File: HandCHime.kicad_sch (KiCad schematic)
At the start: 18 parts, among them J1 USB_C_Receptacle_USB2.0, J2 Pins, SW0 BOOT, SW1 Row 0, Col 0, SW2 Row 0, Col 1, U1 CH552T, U2 USBLC6-2P6

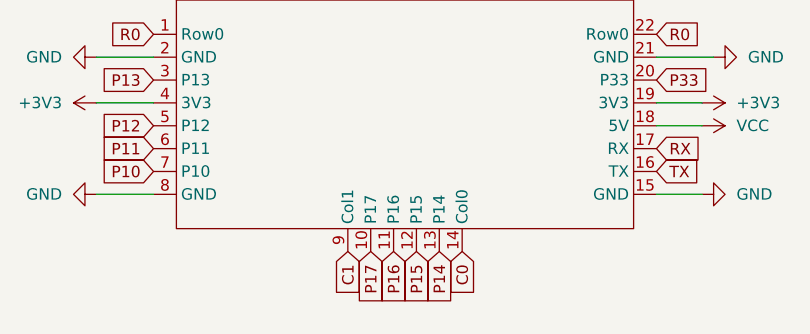
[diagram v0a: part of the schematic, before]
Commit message: Try moving MCU to central part of board
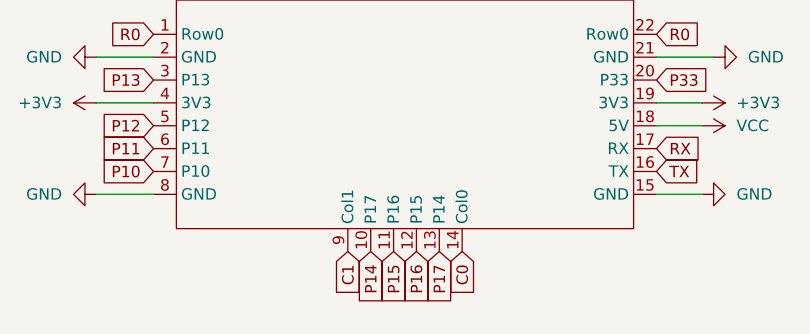
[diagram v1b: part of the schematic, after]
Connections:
- net P14: now also J2.10 (P17); no longer J2.13 (P14)
- net P15: now also J2.11 (P16); no longer J2.12 (P15)
- net P16: now also J2.12 (P15); no longer J2.11 (P16)
- net P17: now also J2.13 (P14); no longer J2.10 (P17)

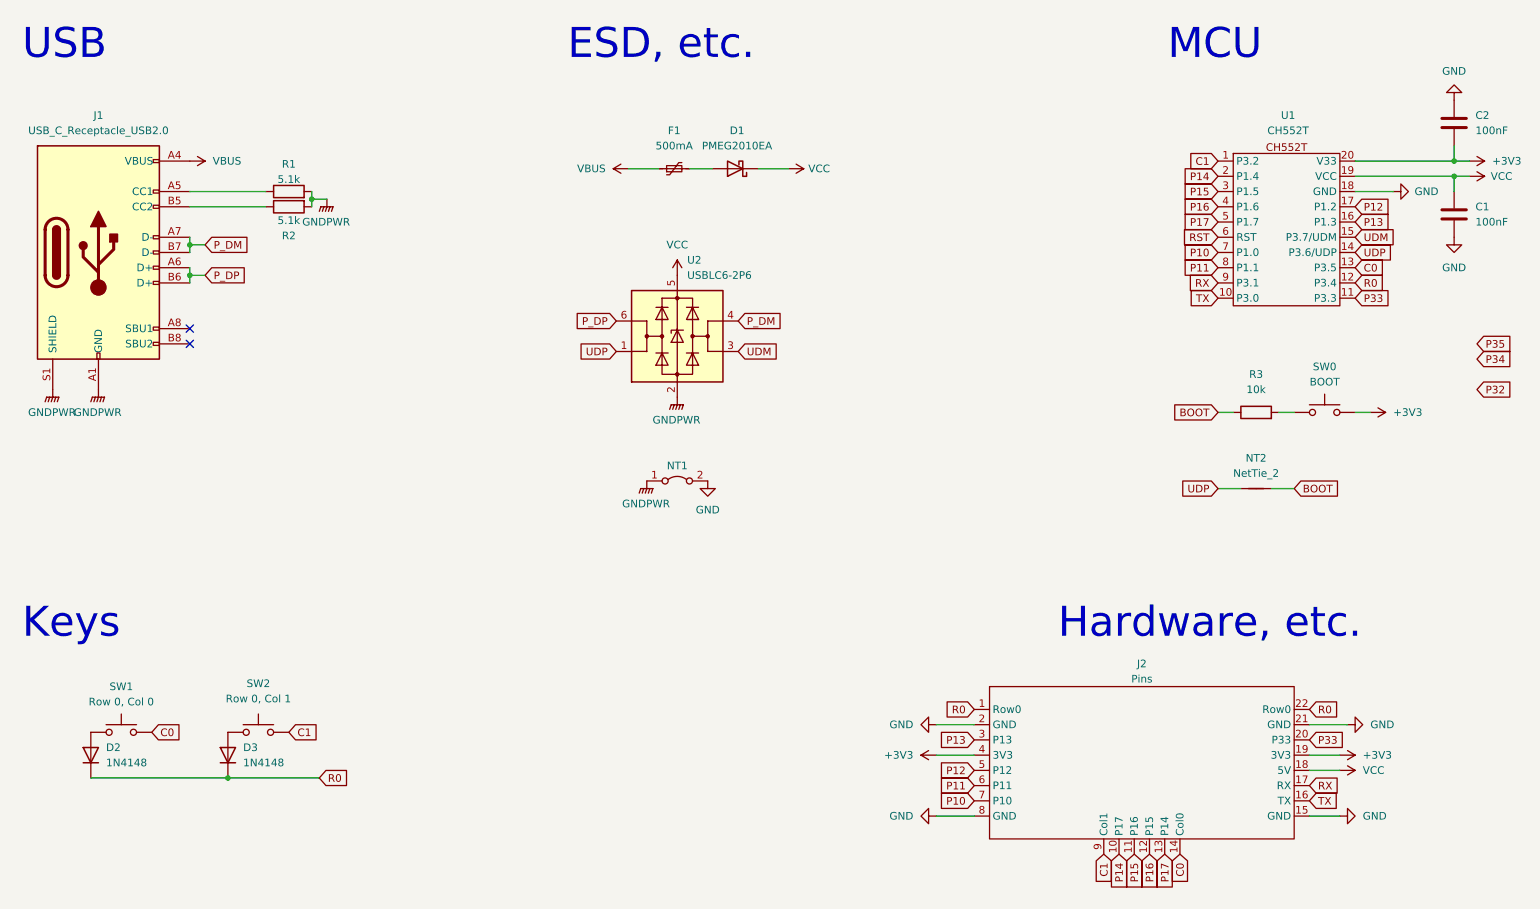
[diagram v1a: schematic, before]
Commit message: Move MCU to centre of board and reroute
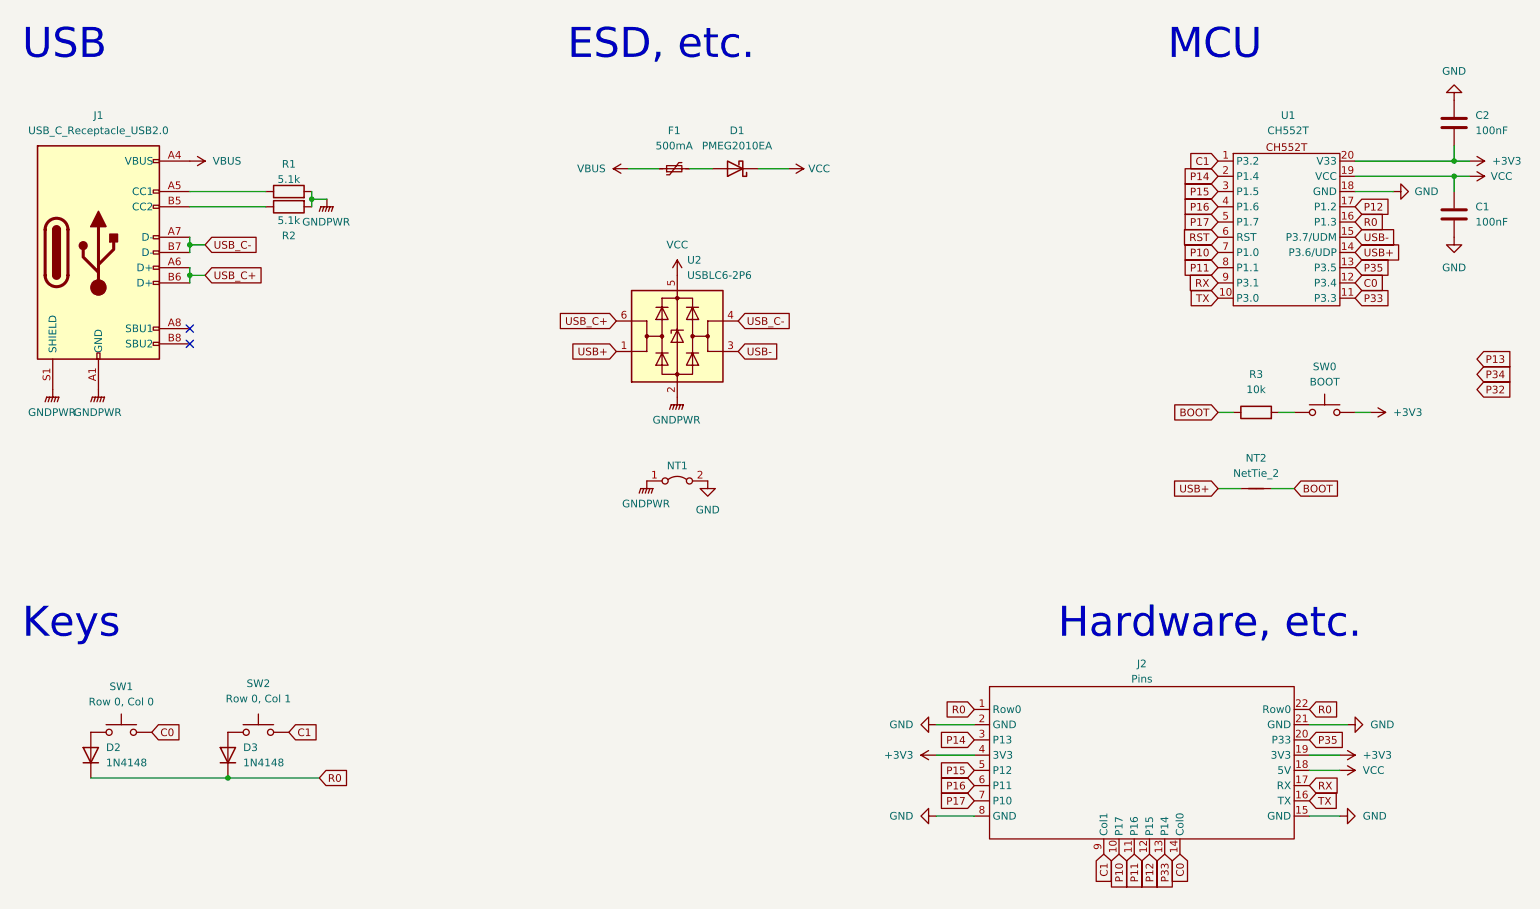
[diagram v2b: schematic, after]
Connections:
- net C0: now also U1.12 (P3.4); no longer U1.13 (P3.5)
- net P10: now also J2.10 (P17); no longer J2.7 (P10)
- net P11: now also J2.11 (P16); no longer J2.6 (P11)
- net P12: now also J2.12 (P15); no longer J2.5 (P12)
- net P13: no longer J2.3 (P13), U1.16 (P1.3)
- net P14: now also J2.3 (P13); no longer J2.10 (P17)
- net P15: now also J2.5 (P12); no longer J2.11 (P16)
- net P16: now also J2.6 (P11); no longer J2.12 (P15)
- net P17: now also J2.7 (P10); no longer J2.13 (P14)
- net P33: now also J2.13 (P14); no longer J2.20 (P33)
- net P35: now also J2.20 (P33), U1.13 (P3.5)
- net R0: now also U1.16 (P1.3); no longer U1.12 (P3.4)
- net P_DM renamed USB_C-
- net P_DP renamed USB_C+
- net UDM renamed USB-
- net UDP renamed USB+

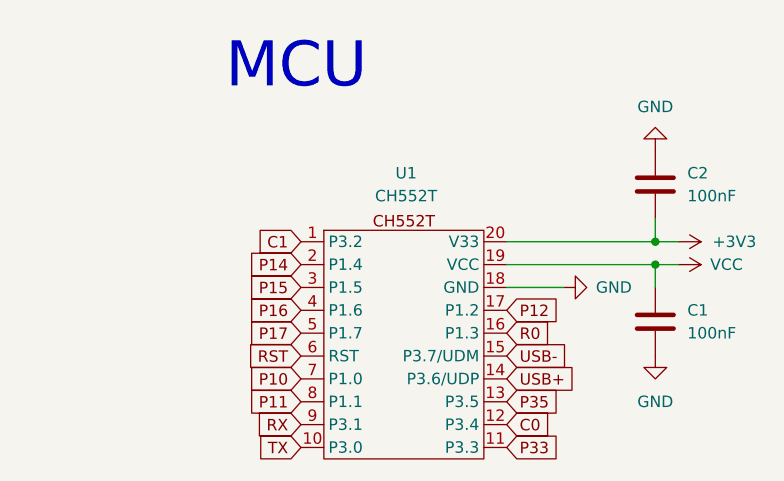
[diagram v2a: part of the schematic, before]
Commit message: Correct CH552 schematic symbols
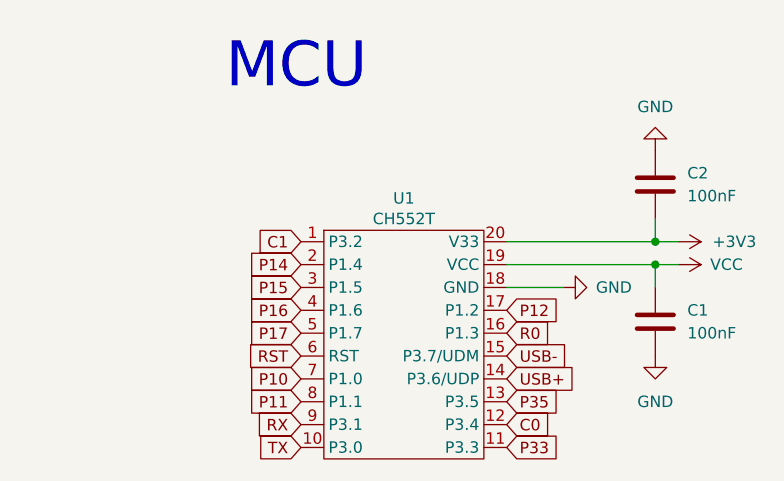
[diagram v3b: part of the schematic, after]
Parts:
- U1: symbol Project Library:MCU_CM552E_MSOP-10 -> Project Library:MCU_CH552T_TSSOP-20
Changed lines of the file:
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@@
 	)
 	(symbol
-		(lib_id "Project Library:MCU_CM552E_MSOP-10")
+		(lib_id "Project Library:MCU_CH552T_TSSOP-20")
 		(at 228.6 48.26 0)
 		(unit 1)
@@
 		(on_board yes)
 		(dnp no)
-		(fields_autoplaced yes)
 		(property "Reference" "U1"
-			(at 228.854 31.75 0)
+			(at 228.6 34.544 0)
 			(effects
 				(font
@@
 		)
 		(property "Value" "CH552T"
-			(at 228.854 34.29 0)
+			(at 228.6 36.83 0)
 			(effects
 				(font
@@
 			)
 		)
-		(property "Datasheet" ""
-			(at 228.6 60.96 0)
+		(property "Datasheet" "https://www.wch-ic.com/downloads/file/309.html"
+			(at 228.6 69.85 0)
 			(effects
 				(font
@@
 		)
 		(property "LCSC" "C111367"
-			(at 228.6 67.056 0)
+			(at 228.6 67.31 0)
 			(effects
 				(font

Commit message: Update net tie in schematic
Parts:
- NT2: footprint NetTie:NetTie-2_SMD_Pad0.5mm -> Project Library:NetTie-2_SMD_Pad0.254mm
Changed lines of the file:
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@@
 			)
 		)
-		(property "Footprint" "NetTie:NetTie-2_SMD_Pad0.5mm"
+		(property "Footprint" "Project Library:NetTie-2_SMD_Pad0.254mm"
 			(at 223.52 93.98 0)
 			(effects

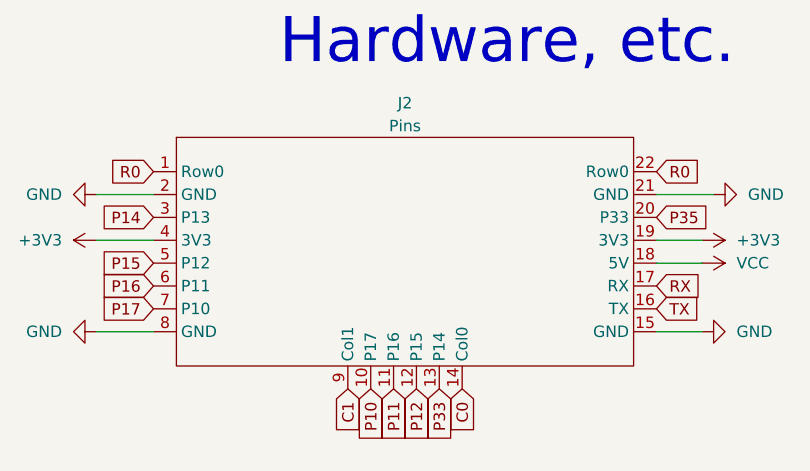
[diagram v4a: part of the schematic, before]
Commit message: Add labels to pins
Labels are currently on the back silkscreen, which is not the best. However, trying to squeeze them on the front seems optimistic.
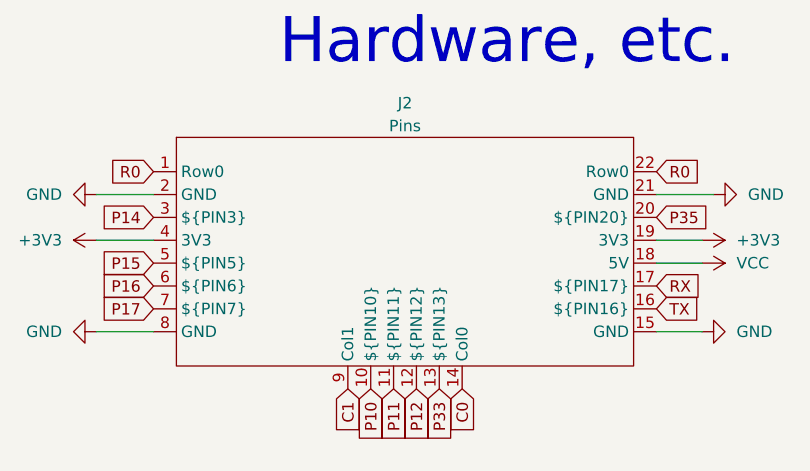
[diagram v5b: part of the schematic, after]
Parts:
- J2: PIN10 (none) -> 10; PIN11 (none) -> 11; PIN12 (none) -> 12; PIN13 (none) -> 33; PIN16 (none) -> 30(TX); PIN17 (none) -> 31(RX); PIN20 (none) -> 35; PIN3 (none) -> 14; PIN5 (none) -> 15; PIN6 (none) -> 16; PIN7 (none) -> 17
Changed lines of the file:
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@@
+			)
+		)
+		(property "PIN3" "14"
+			(at 204.47 139.7 0)
+			(effects
+				(font
+					(size 1.27 1.27)
+				)
+				(hide yes)
+			)
+		)
+		(property "PIN5" "15"
+			(at 204.47 139.7 0)
+			(effects
+				(font
+					(size 1.27 1.27)
+				)
+				(hide yes)
+			)
+		)
+		(property "PIN6" "16"
+			(at 204.47 139.7 0)
+			(effects
+				(font
+					(size 1.27 1.27)
+				)
+				(hide yes)
+			)
+		)
+		(property "PIN7" "17"
+			(at 204.47 139.7 0)
+			(effects
+				(font
+					(size 1.27 1.27)
+				)
+				(hide yes)
+			)
+		)
+		(property "PIN10" "10"
+			(at 204.47 139.7 0)
+			(effects
+				(font
+					(size 1.27 1.27)
+				)
+				(hide yes)
+			)
+		)
+		(property "PIN11" "11"
+			(at 204.47 139.7 0)
+			(effects
+				(font
+					(size 1.27 1.27)
+				)
+				(hide yes)
+			)
+		)
+		(property "PIN12" "12"
+			(at 204.47 139.7 0)
+			(effects
+				(font
+					(size 1.27 1.27)
+				)
+				(hide yes)
+			)
+		)
+		(property "PIN13" "33"
+			(at 204.47 139.7 0)
+			(effects
+				(font
+					(size 1.27 1.27)
+				)
+				(hide yes)
+			)
+		)
+		(property "PIN16" "30(TX)"
+			(at 204.47 139.7 0)
+			(effects
+				(font
+					(size 1.27 1.27)
+				)
+				(hide yes)
+			)
+		)
+		(property "PIN17" "31(RX)"
+			(at 204.47 139.7 0)
+			(effects
+				(font
+					(size 1.27 1.27)
+				)
+				(hide yes)
+			)
+		)
+		(property "PIN20" "35"
+			(at 204.47 139.7 0)
+			(effects
+				(font
+					(size 1.27 1.27)
+				)
+				(hide yes)
 			)
 		)

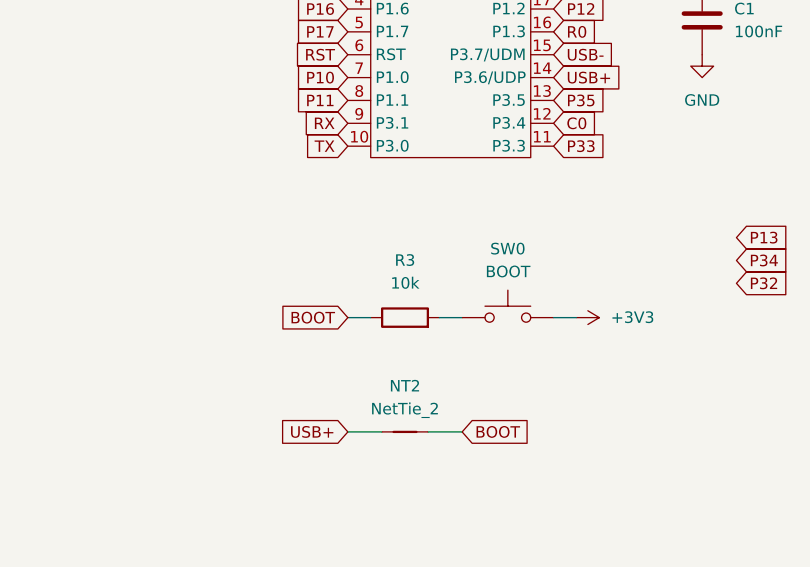
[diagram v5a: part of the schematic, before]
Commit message: Update boot switch
 * Now uses the smaller B3U-1000P switch
 * Alternate pads provided on the keyswitch side so that Boot can be accessed by removing a keycap and poking through LED slot (on compatible switches)
 * Can now reroute C0 to avoid snaking around too much
 * Took advantage of now smaller vias on other traces
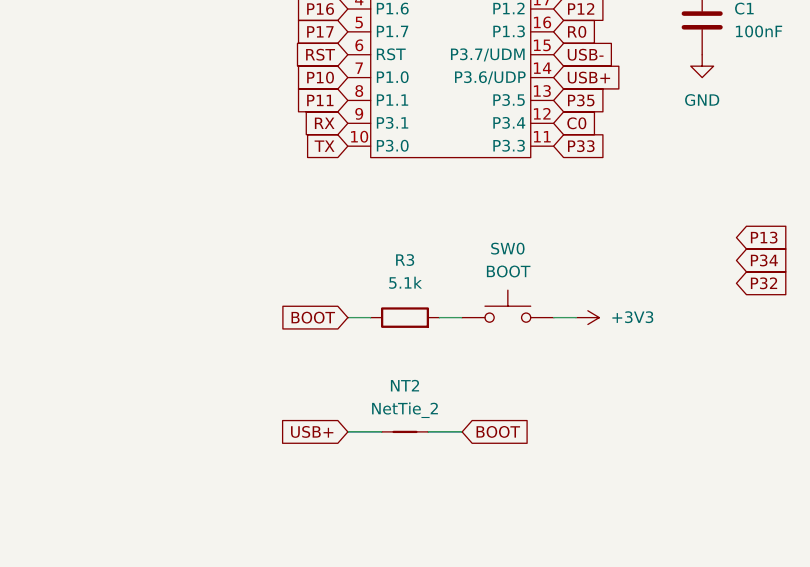
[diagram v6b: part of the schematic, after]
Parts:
- R3: value 10k -> 5.1k
- SW0: footprint PCM_marbastlib-various:SW_SPST_SKQG_WithStem -> Project Library:SW_SPST_B3U-1000P
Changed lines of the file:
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@@
 			)
 		)
-		(property "Value" "10k"
+		(property "Value" "5.1k"
 			(at 223.52 77.47 90)
 			(effects
@@
 			)
 		)
-		(property "Footprint" "PCM_marbastlib-various:SW_SPST_SKQG_WithStem"
+		(property "Footprint" "Project Library:SW_SPST_B3U-1000P"
 			(at 234.95 76.2 0)
 			(effects

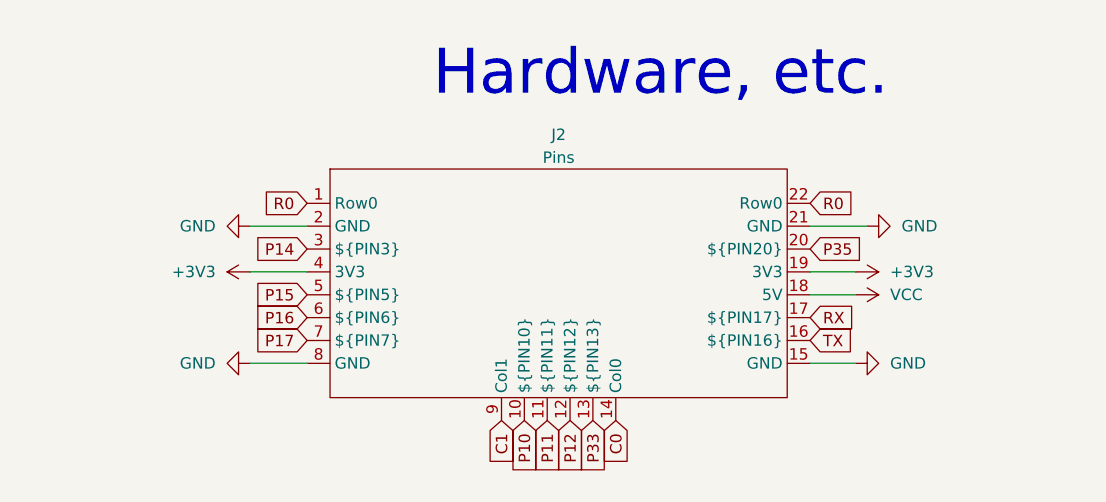
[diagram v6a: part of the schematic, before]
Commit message: Swap +5 and 3.3V outputs
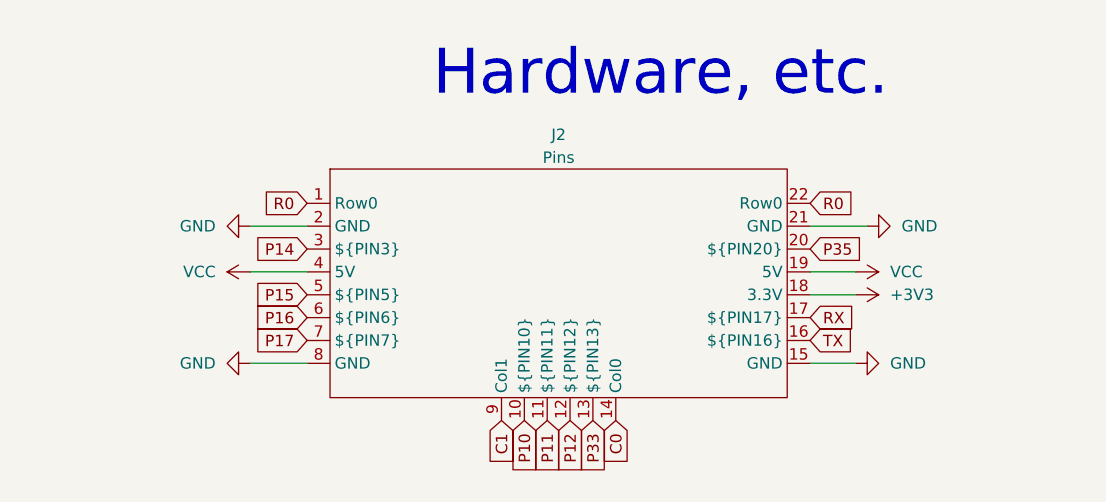
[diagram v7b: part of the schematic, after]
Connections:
- net +3V3: now also J2.18 (3.3V); no longer J2.19 (3V3), J2.4 (3V3)
- net VCC: now also J2.19 (5V), J2.4 (5V); no longer J2.18 (5V)
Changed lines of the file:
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@@
 	(symbol
 		(lib_id "power:+3V3")
-		(at 237.49 138.43 270)
-		(mirror x)
+		(at 237.49 140.97 270)
 		(unit 1)
 		(exclude_from_sim no)
@@
 		(dnp no)
 		(property "Reference" "#PWR011"
-			(at 233.68 138.43 0)
+			(at 233.68 140.97 0)
 			(effects
 				(font
@@
 		)
 		(property "Value" "+3V3"
-			(at 241.3 138.4299 90)
+			(at 241.3 140.9701 90)
 			(effects
 				(font
@@
 		)
 		(property "Footprint" ""
-			(at 237.49 138.43 0)
+			(at 237.49 140.97 0)
 			(effects
 				(font
@@
 		)
 		(property "Datasheet" ""
-			(at 237.49 138.43 0)
+			(at 237.49 140.97 0)
 			(effects
 				(font
@@
 		)
 		(property "Description" ""
-			(at 237.49 138.43 0)
+			(at 237.49 140.97 0)
 			(effects
 				(font
@@
 	)
 	(symbol
+		(lib_id "power:+5V")
+		(at 170.18 138.43 90)
+		(unit 1)
+		(exclude_from_sim no)
+		(in_bom yes)
+		(on_board yes)
+		(dnp no)
+		(property "Reference" "#PWR017"
+			(at 173.99 138.43 0)
+			(effects
+				(font
+					(size 1.27 1.27)
+				)
+				(hide yes)
+			)
+		)
+		(property "Value" "VCC"
+			(at 166.37 138.4299 90)
+			(effects
+				(font
+					(size 1.27 1.27)
+				)
+				(justify left)
+			)
+		)
+		(property "Footprint" ""
+			(at 170.18 138.43 0)
+			(effects
+				(font
+					(size 1.27 1.27)
+				)
+				(hide yes)
+			)
+		)
+		(property "Datasheet" ""
+			(at 170.18 138.43 0)
+			(effects
+				(font
+					(size 1.27 1.27)
+				)
+				(hide yes)
+			)
+		)
+		(property "Description" "Power symbol creates a global label with name \"+5V\""
+			(at 170.18 138.43 0)
+			(effects
+				(font
+					(size 1.27 1.27)
+				)
+				(hide yes)
+			)
+		)
+		(pin "1"
+		)
+		(instances
+			(project "HandCHime"
+				(path "/34400e51-cf83-464a-b3ec-e9a28a972a27"
+					(reference "#PWR017")
+					(unit 1)
+				)
+			)
+		)
+	)
+	(symbol
 		(lib_id "Power_Protection:USBLC6-2SC6")
 		(at 127 68.58 0)
@@
 	(symbol
 		(lib_id "power:+5V")
-		(at 237.49 140.97 270)
-		(mirror x)
+		(at 237.49 138.43 270)
 		(unit 1)
 		(exclude_from_sim no)
@@
 		(dnp no)
 		(property "Reference" "#PWR010"
-			(at 233.68 140.97 0)
+			(at 233.68 138.43 0)
 			(effects
 				(font
@@
 		)
 		(property "Value" "VCC"
-			(at 241.3 140.9699 90)
+			(at 241.3 138.4301 90)
 			(effects
 				(font
@@
 		)
 		(property "Footprint" ""
-			(at 237.49 140.97 0)
+			(at 237.49 138.43 0)
 			(effects
 				(font
@@
 		)
 		(property "Datasheet" ""
-			(at 237.49 140.97 0)
+			(at 237.49 138.43 0)
 			(effects
 				(font
@@
 		)
 		(property "Description" "Power symbol creates a global label with name \"+5V\""
-			(at 237.49 140.97 0)
+			(at 237.49 138.43 0)
 			(effects
 				(font
@@
 					(unit 1)
 				)
-			)
-		)
-	)
-	(symbol
-		(lib_id "power:+3V3")
-		(at 170.18 138.43 90)
-		(unit 1)
-		(exclude_from_sim no)
-		(in_bom yes)
-		(on_board yes)
-		(dnp no)
-		(fields_autoplaced yes)
-		(property "Reference" "#PWR017"
-			(at 173.99 138.43 0)
-			(effects
-				(font
-					(size 1.27 1.27)
-				)
-				(hide yes)
-			)
-		)
-		(property "Value" "+3V3"
-			(at 166.37 138.4299 90)
-			(effects
-				(font
-					(size 1.27 1.27)
-				)
-				(justify left)
-			)
-		)
-		(property "Footprint" ""
-			(at 170.18 138.43 0)
-			(effects
-				(font
-					(size 1.27 1.27)
-				)
-				(hide yes)
-			)
-		)
-		(property "Datasheet" ""
-			(at 170.18 138.43 0)
-			(effects
-				(font
-					(size 1.27 1.27)
-				)
-				(hide yes)
-			)
-		)
-		(property "Description" ""
-			(at 170.18 138.43 0)
-			(effects
-				(font
-					(size 1.27 1.27)
-				)
-				(hide yes)
-			)
-		)
-		(pin "1"
-		)
-		(instances
-			(project "HandCHime"
-				(path "/34400e51-cf83-464a-b3ec-e9a28a972a27"
-					(reference "#PWR017")
-					(unit 1)
-				)
